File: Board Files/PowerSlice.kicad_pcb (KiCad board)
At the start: 2 copper layers, 100 x 70 mm, 49 parts, among them J1 Conn_01x10_Pin, J3 DC_In_Screw, J4 ESTOP, U1 PTH08080WAD, U2 PTH08080WAD, U3 INA214BIDCKR, U4 INA214BIDCKR, U5 INA214BIDCKR, U6 NUCLEO-F303K8

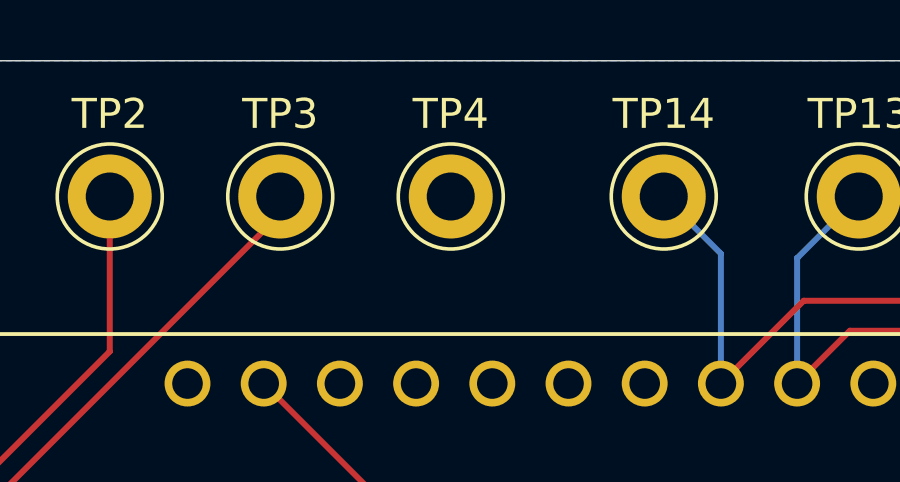
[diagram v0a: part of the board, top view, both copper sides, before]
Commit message: Updated to KiCAD 10, fancified schematic for final presentation, verified ERC and DRC still good
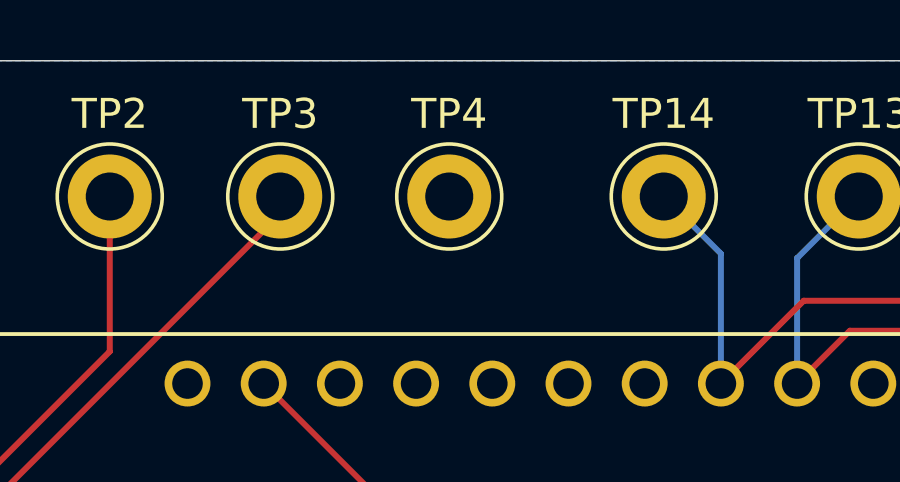
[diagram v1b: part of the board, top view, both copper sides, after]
